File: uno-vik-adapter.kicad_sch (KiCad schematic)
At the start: 8 parts, among them J1 Power, J2 Digital/PWM, J3 Analog, J4 Digital/PWM

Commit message: Tweaks.
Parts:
- J5, J6: LCSC Part Number (none) -> C479750
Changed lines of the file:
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@@
+			)
+		)
+		(property "LCSC Part Number" "C479750"
+			(at 198.12 49.53 0)
+			(effects
+				(font
+					(size 1.27 1.27)
+				)
+				(hide yes)
 			)
 		)
@@
 			(at 153.67 49.53 0)
 			(effects
+				(font
+					(size 1.27 1.27)
+				)
+				(hide yes)
+			)
+		)
+		(property "LCSC Part Number" "C479750"
+			(at 153.67 49.53 0)
+			(effects

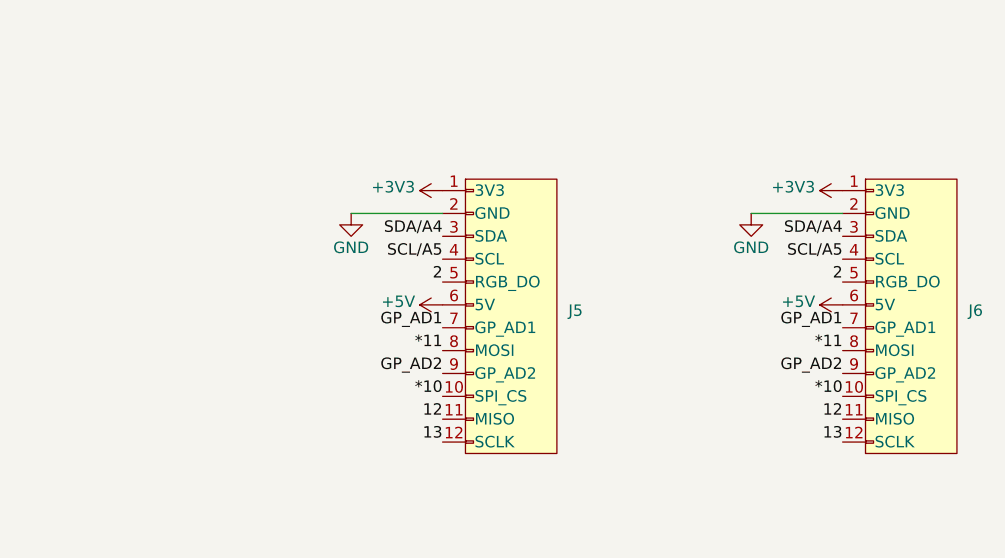
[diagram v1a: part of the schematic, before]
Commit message: Add jumpers for 5v pin.
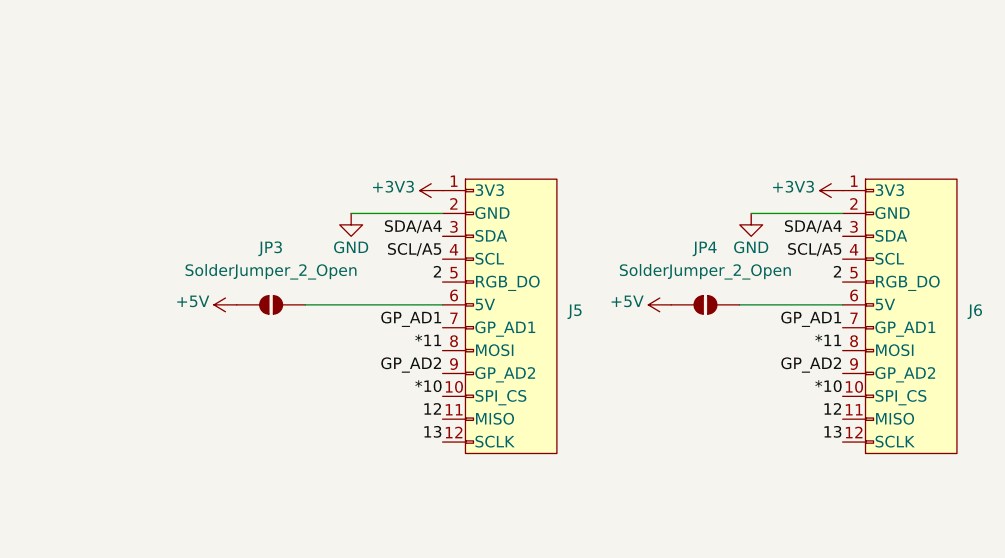
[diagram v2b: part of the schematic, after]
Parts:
- added JP3, JP4: SolderJumper_2_Open, Jumper:SolderJumper-2_P1.3mm_Open_TrianglePad1.0x1.5mm, symbol Jumper:SolderJumper_2_Open
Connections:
- net +5V: now also JP3.1 (A), JP4.1 (A); no longer J5.6 (5V), J6.6 (5V)
- new net: J6.6 (5V), JP4.2 (B)
- new net: J5.6 (5V), JP3.2 (B)
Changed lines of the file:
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@@
+	(wire
+		(pts
+			(xy 179.07 49.53) (xy 190.5 49.53)
+		)
+		(stroke
+			(width 0)
+			(type default)
+		)
+	)
+	(wire
+		(pts
+			(xy 130.81 49.53) (xy 146.05 49.53)
+		)
+		(stroke
+			(width 0)
+			(type default)
+		)
+	)
 	(wire
 		(pts
@@
 	)
 	(symbol
+		(lib_id "Jumper:SolderJumper_2_Open")
+		(at 127 49.53 0)
+		(unit 1)
+		(exclude_from_sim yes)
+		(in_bom no)
+		(on_board yes)
+		(dnp no)
+		(fields_autoplaced yes)
+		(property "Reference" "JP3"
+			(at 127 43.18 0)
+			(effects
+				(font
+					(size 1.27 1.27)
+				)
+			)
+		)
+		(property "Value" "SolderJumper_2_Open"
+			(at 127 45.72 0)
+			(effects
+				(font
+					(size 1.27 1.27)
+				)
+			)
+		)
+		(property "Footprint" "Jumper:SolderJumper-2_P1.3mm_Open_TrianglePad1.0x1.5mm"
+			(at 127 49.53 0)
+			(effects
+				(font
+					(size 1.27 1.27)
+				)
+				(hide yes)
+			)
+		)
+		(property "Datasheet" "~"
+			(at 127 49.53 0)
+			(effects
+				(font
+					(size 1.27 1.27)
+				)
+				(hide yes)
+			)
+		)
+		(property "Description" "Solder Jumper, 2-pole, open"
+			(at 127 49.53 0)
+			(effects
+				(font
+					(size 1.27 1.27)
+				)
+				(hide yes)
+			)
+		)
+		(pin "2"
+		)
+		(pin "1"
+		)
+		(instances
+			(project ""
+				(path "/e63e39d7-6ac0-4ffd-8aa3-1841a4541b55"
+					(reference "JP3")
+					(unit 1)
+				)
+			)
+		)
+	)
+	(symbol
 		(lib_id "power:VCC")
 		(at 26.67 26.67 0)
@@
 	(symbol
 		(lib_id "power:+5V")
-		(at 190.5 49.53 90)
+		(at 171.45 49.53 90)
 		(unit 1)
 		(exclude_from_sim no)
@@
 		(dnp no)
 		(property "Reference" "#PWR011"
-			(at 194.31 49.53 0)
+			(at 175.26 49.53 0)
 			(effects
 				(font
@@
 		)
 		(property "Value" "+5V"
-			(at 187.452 49.1744 90)
+			(at 168.402 49.1744 90)
 			(effects
 				(font
@@
 		)
 		(property "Footprint" ""
-			(at 190.5 49.53 0)
+			(at 171.45 49.53 0)
 			(effects
 				(font
@@
 		)
 		(property "Datasheet" ""
-			(at 190.5 49.53 0)
+			(at 171.45 49.53 0)
 			(effects
 				(font
@@
 		)
 		(property "Description" ""
-			(at 190.5 49.53 0)
+			(at 171.45 49.53 0)
 			(effects
 				(font
@@
 	)
 	(symbol
+		(lib_id "Jumper:SolderJumper_2_Open")
+		(at 175.26 49.53 0)
+		(unit 1)
+		(exclude_from_sim yes)
+		(in_bom no)
+		(on_board yes)
+		(dnp no)
+		(fields_autoplaced yes)
+		(property "Reference" "JP4"
+			(at 175.26 43.18 0)
+			(effects
+				(font
+					(size 1.27 1.27)
+				)
+			)
+		)
+		(property "Value" "SolderJumper_2_Open"
+			(at 175.26 45.72 0)
+			(effects
+				(font
+					(size 1.27 1.27)
+				)
+			)
+		)
+		(property "Footprint" "Jumper:SolderJumper-2_P1.3mm_Open_TrianglePad1.0x1.5mm"
+			(at 175.26 49.53 0)
+			(effects
+				(font
+					(size 1.27 1.27)
+				)
+				(hide yes)
+			)
+		)
+		(property "Datasheet" "~"
+			(at 175.26 49.53 0)
+			(effects
+				(font
+					(size 1.27 1.27)
+				)
+				(hide yes)
+			)
+		)
+		(property "Description" "Solder Jumper, 2-pole, open"
+			(at 175.26 49.53 0)
+			(effects
+				(font
+					(size 1.27 1.27)
+				)
+				(hide yes)
+			)
+		)
+		(pin "2"
+		)
+		(pin "1"
+		)
+		(instances
+			(project "uno-vik-adapter"
+				(path "/e63e39d7-6ac0-4ffd-8aa3-1841a4541b55"
+					(reference "JP4")
+					(unit 1)
+				)
+			)
+		)
+	)
+	(symbol
 		(lib_id "power:+5V")
-		(at 146.05 49.53 90)
+		(at 123.19 49.53 90)
 		(unit 1)
 		(exclude_from_sim no)
@@
 		(dnp no)
 		(property "Reference" "#PWR07"
-			(at 149.86 49.53 0)
+			(at 127 49.53 0)
 			(effects
 				(font
@@
 		)
 		(property "Value" "+5V"
-			(at 143.002 49.1744 90)
+			(at 120.142 49.1744 90)
 			(effects
 				(font
@@
 		)
 		(property "Footprint" ""
-			(at 146.05 49.53 0)
+			(at 123.19 49.53 0)
 			(effects
 				(font
@@
 		)
 		(property "Datasheet" ""
-			(at 146.05 49.53 0)
+			(at 123.19 49.53 0)
 			(effects
 				(font
@@
 		)
 		(property "Description" ""
-			(at 146.05 49.53 0)
-			(effects
-				(font
+			(at 123.19 49.53 0)
+			(effects
+				(font
